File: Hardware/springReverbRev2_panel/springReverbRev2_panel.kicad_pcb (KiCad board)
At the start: 2 copper layers, 100 x 200 mm, 21 parts

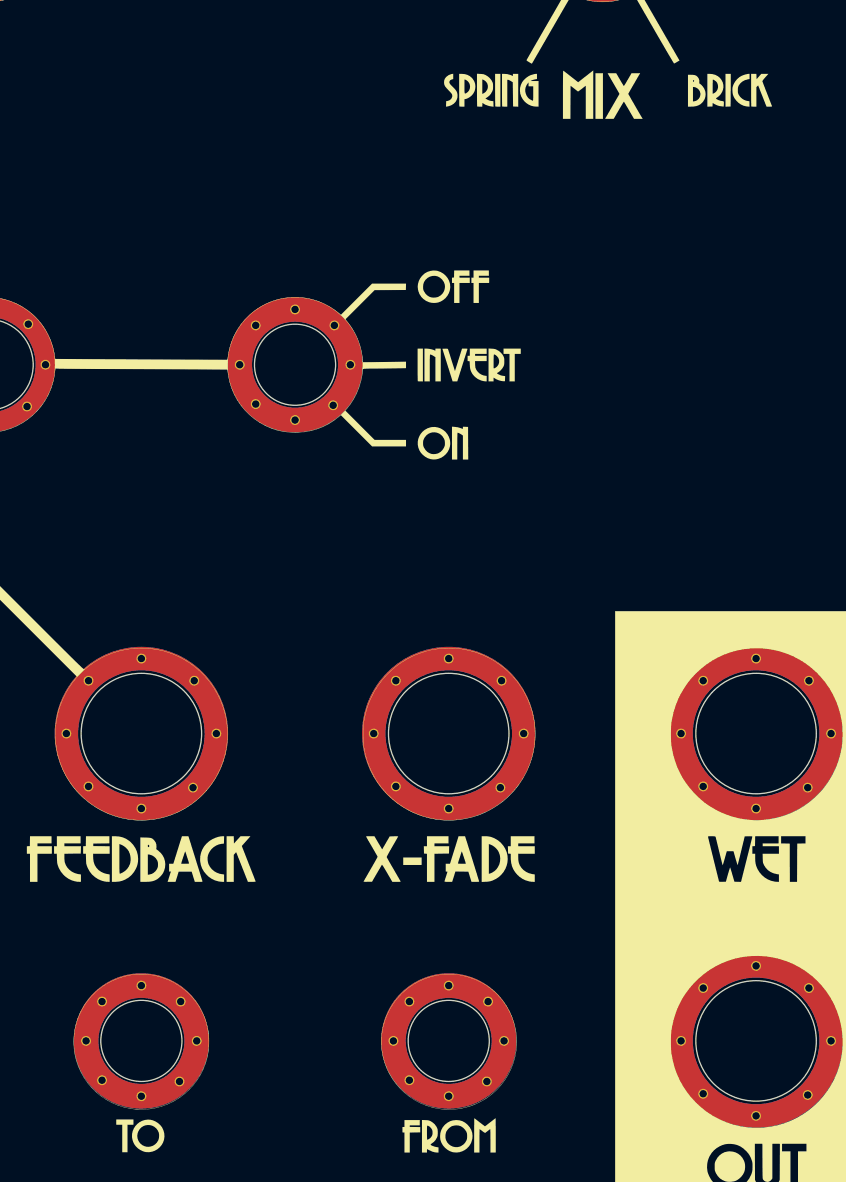
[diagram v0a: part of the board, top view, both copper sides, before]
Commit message: Ungrounded jack
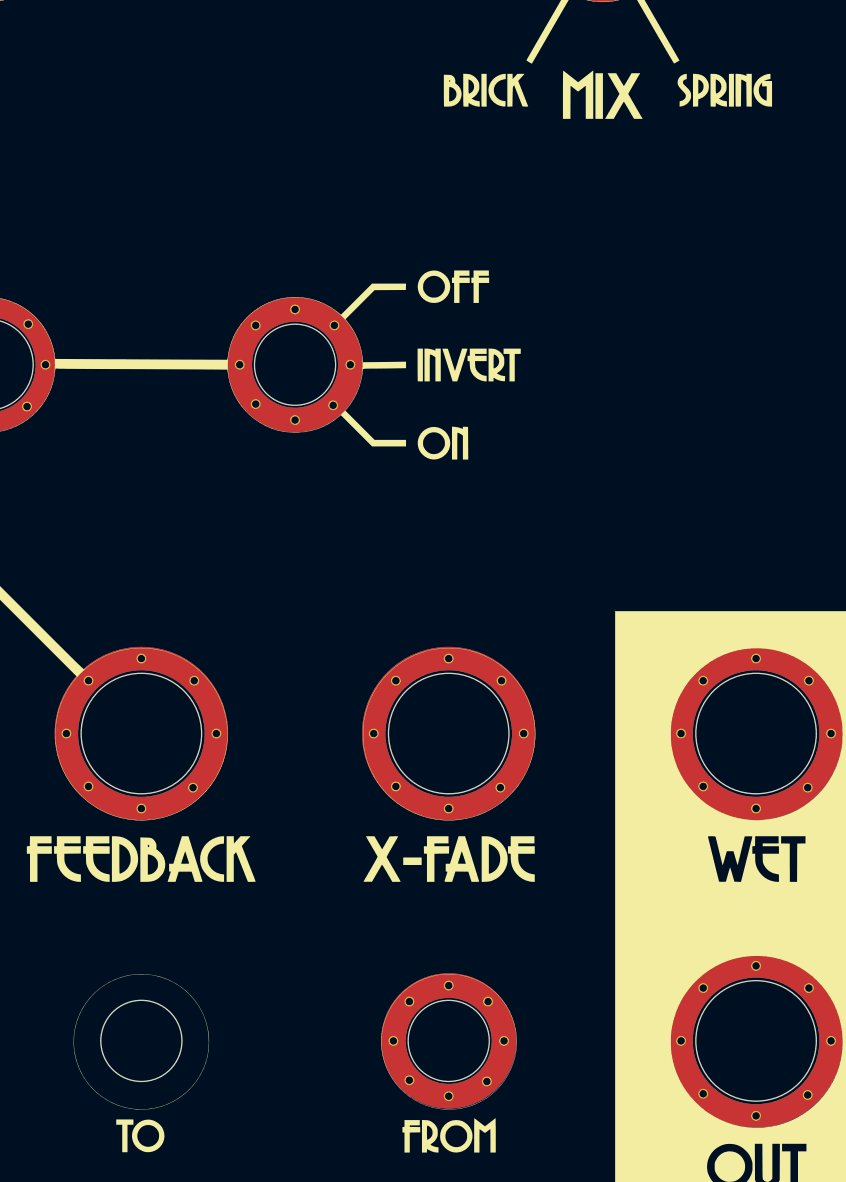
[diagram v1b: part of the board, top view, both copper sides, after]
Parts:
- H18: value RCA_Jack_Hole -> Nongrounded_Jack_Hole; footprint springReverbRev2_panel:Kosmo_RCA_Jack_Hole -> springReverbRev2_panel:Kosmo_Nongrounded_RCA_Jack_Hole
- moved H17 25.0 mm to (128.6, 232.6)
- moved H18 25.0 mm to (103.6, 232.6)
